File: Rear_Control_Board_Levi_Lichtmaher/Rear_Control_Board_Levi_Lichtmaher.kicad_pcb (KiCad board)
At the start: 2 copper layers, 149.2 x 106.5 mm, 92 parts, among them J1 430450200, J10 Molex Micro-Fit 4 Pin, J11 22035035, J12 22035035, J2 430450200, J3 430450200, J4 430450200, J5 430450200, J6 430450200, J7 430450200, J8 430450200, J9 22035035, Q1 PSMN1R8-40YLC_115, Q2 PSMN1R8-40YLC_115, Q3 PSMN1R8-40YLC_115, Q4 PSMN1R8-40YLC_115, U11 MCP6286T-E/OT, U12 MCP6286T-E/OT, U3 MCP2562-E/P, U4 UA78M05QDCYRG4Q1, U5 ASM330LHHTR, U6 MCP6286T-E/OT

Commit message: implemented feedback
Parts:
- added R22: 2K, Resistor_SMD:R_0805_2012Metric, F.Cu at (187.3, 102.3)
- added R23: 1K, Resistor_SMD:R_0805_2012Metric, F.Cu at (187.3, 98.7)
- TP35: value 2V5 -> 2V2
- moved TP35 76.2 mm to (189.6, 99.7)
- moved C1 10.2 mm to (103.0, 52.0), turned to 90 degrees
- moved C3 8.67 mm to (99.3, 52.7)
- moved TP15 5.20 mm to (200.1, 92.8)
- moved TP18 4.79 mm to (188.0, 108.3)
- moved TP7 4.13 mm to (96.0, 55.0)
- moved U4 2.22 mm to (100.7, 58.1), turned to 180 degrees
- moved J2 0.77 mm to (191.6, 46.9)
- moved C2 0.71 mm to (181.1, 104.8)
- moved R17 0.67 mm to (179.1, 104.9)
- moved U2 0.49 mm to (179.9, 109.8)
- moved R19 0.35 mm to (180.5, 100.5)
- moved R12 0.05 mm to (180.5, 98.5)
- renumbered 3.3V to TP12, 2.4V to TP18, 5V to TP2, 2.4V to TP21, 12V to TP27, 12V to TP36, GND to TP43, ADC to U2
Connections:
- net +2V5 renamed Net-(U2-AIN3)
- U4 pad 1: +5V -> +12V
- U4 pad 3: +12V -> +5V
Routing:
- net Net-(U2-AIN3): track 0.00 -> 15.6 mm
- net /MISO: track 1.90 -> 14.5 mm
- net +5V: track 135.4 -> 142.6 mm
- net /SCK: track 39.4 -> 33.9 mm, vias 2 -> 0
- net Net-(U7-PB14): track 12.3 -> 8.14 mm
- net +3V3: track 283.9 -> 280.1 mm
- net /Pressure: track 25.7 -> 29.0 mm
- net +12V: track 276.1 -> 273.2 mm
- net Net-(J9-Pad3): track 9.61 -> 6.70 mm
- net GND: track 81.4 -> 79.7 mm, vias 37 -> 38
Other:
- board text added: "2.2V"
- board text added: "2.4V"
- board text added: "3.3V"
- board text added: "LDO"
- board text added: "MOSFET"
- board text added: "TP7"
- board text removed: "IDK what to do with this and IDK where to get 2.5V"
- board text removed: "TP12"
- board text removed: "TP18"
- board text removed: "TP2"
- board text removed: "TP21"
- board text removed: "TP27"
- board text removed: "TP36"
- board text removed: "TP43"

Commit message: made board smaller, cleaned up silkscreen
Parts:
- moved REF** 70.8 mm to (78.2, 64.0)
- moved H4 19.4 mm to (207.0, 121.0)
- moved H3 19.0 mm to (74.0, 121.0)
- moved TP37 15.3 mm to (180.8, 52.7)
- moved C19 6.55 mm to (186.3, 84.0)
- moved C22 6.55 mm to (182.3, 86.5)
- moved R9 6.55 mm to (185.8, 87.5)
- moved U6 6.55 mm to (189.3, 86.2)
- moved C7 6.55 mm to (193.3, 84.5)
- moved R15 6.55 mm to (192.3, 90.4)
- moved R16 6.55 mm to (188.3, 90.4)
- moved J9 6.55 mm to (197.8, 85.4)
- moved TP14 6.55 mm to (192.5, 87.5)
- moved TP15 6.55 mm to (193.6, 92.4)
- moved H2 4.11 mm to (207.0, 46.5)
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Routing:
- net +12V: track 273.2 -> 260.4 mm
- net +5V: track 142.6 -> 136.5 mm
- net +3V3: track 280.1 -> 276.9 mm
- net GND: track 79.7 -> 82.8 mm
- net /Pressure: track 29.0 -> 32.1 mm
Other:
- board size 149.2 x 106.5 mm -> 143.7 x 84.4 mm
- board text added: "ADC"
- board text added: "CAN Tranciever"
- board text added: "Rear Control Board 01/03/2025 University of California, Los Angeles By Levi Lichtmaher"
- board text removed: "Rear Control Board 12/27/2025 University of California, Los Angeles By Levi Lichtmaher"
- board text removed: "This feels like empty space can i put cool images here or smth"

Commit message: cleaned some stuff up
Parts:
- moved TP43 0.45 mm to (90.2, 51.2)
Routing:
- net GND: track 82.8 -> 81.4 mm, vias 38 -> 37
- net +12V: track 260.4 -> 261.1 mm
- net +3V3: track 276.9 -> 277.5 mm
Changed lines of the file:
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@@
 	(footprint "TestPoint:TestPoint_Pad_D1.0mm"
 		(layer "F.Cu")
-		(at 90.649999 51.25)
+		(at 90.2 51.25)
 		(descr "SMD pad as test Point, diameter 1.0mm")
 		(tags "test point SMD pad")
@@
 	)
 	(segment
-		(start 87.200001 45.825)
-		(end 88.800001 44.225)
-		(width 1)
-		(layer "F.Cu")
-		(net 1)
-	)
-	(segment
 		(start 87.200001 91.1416)
 		(end 87.200001 100.175)
@@
 	)
 	(segment
-		(start 101.549 53.3735)
-		(end 102.975 54.7995)
-		(width 1)
-		(layer "F.Cu")
-		(net 1)
-	)
-	(segment
 		(start 87.200001 73.175)
 		(end 87.200001 81.6416)
@@
 	)
 	(segment
-		(start 88.800001 44.225)
-		(end 98.276844 44.225)
+		(start 89.600001 43.425)
+		(end 97.476844 43.425)
 		(width 1)
 		(layer "F.Cu")
@@
 	)
 	(segment
+		(start 101.549 47.497156)
+		(end 101.549 53.3735)
+		(width 1)
+		(layer "F.Cu")
+		(net 1)
+	)
+	(segment
 		(start 199.57205 52.14705)
 		(end 203.5 56.075)
@@
 	)
 	(segment
+		(start 87.200001 45.825)
+		(end 89.600001 43.425)
+		(width 1)
+		(layer "F.Cu")
+		(net 1)
+	)
+	(segment
 		(start 203.5 56.075)
 		(end 203.5 94)
@@
 	)
 	(segment
-		(start 101.549 47.497156)
-		(end 101.549 53.3735)
+		(start 203.5 94)
+		(end 201 96.5)
 		(width 1)
 		(layer "F.Cu")
@@
 	)
 	(segment
-		(start 203.5 94)
-		(end 201 96.5)
+		(start 97.476844 43.425)
+		(end 101.549 47.497156)
+		(width 1)
+		(layer "F.Cu")
+		(net 1)
+	)
+	(segment
+		(start 101.549 53.3735)
+		(end 102.975 54.7995)
 		(width 1)
 		(layer "F.Cu")
@@
 	)
 	(segment
-		(start 98.276844 44.225)
-		(end 101.549 47.497156)
-		(width 1)
-		(layer "F.Cu")
-		(net 1)
-	)
-	(segment
 		(start 87.200001 68)
 		(end 87.200001 73.175)
@@
 	)
 	(segment
-		(start 181.480174 94.480174)
-		(end 181.480174 94.966511)
-		(width 0.2)
-		(layer "F.Cu")
-		(net 2)
-	)
-	(segment
 		(start 100.25 52.675)
 		(end 100.25 54.54355)
@@
 	)
 	(segment
-		(start 90.649999 45.825)
-		(end 90.649999 51.25)
+		(start 90.2 45.825)
+		(end 90.2 51.25)
 		(width 0.2)
 		(layer "F.Cu")
@@
 	)
 	(segment
-		(start 180.042924 95.24685)
-		(end 181.462498 95.24685)
-		(width 0.2)
-		(layer "F.Cu")
-		(net 2)
-	)
-	(segment
 		(start 200.712501 115.6)
 		(end 200.7 115.587499)
@@
 	)
 	(segment
-		(start 181 94)
-		(end 181.480174 94.480174)
-		(width 0.2)
-		(layer "F.Cu")
-		(net 2)
-	)
-	(segment
 		(start 181.9803 94.966511)
 		(end 181.480174 94.966511)
@@
 	)
 	(segment
+		(start 181.480174 94.480174)
+		(end 181.480174 94.966511)
+		(width 0.2)
+		(layer "F.Cu")
+		(net 2)
+	)
+	(segment
 		(start 100.25 54.54355)
 		(end 100.6636 54.95715)
@@
 	)
 	(segment
+		(start 181 94)
+		(end 181.480174 94.480174)
+		(width 0.2)
+		(layer "F.Cu")
+		(net 2)
+	)
+	(segment
 		(start 100.025 51.05)
 		(end 100.225 51.25)
@@
 	)
 	(via
-		(at 181.462498 95.24685)
-		(size 0.6)
-		(drill 0.3)
-		(layers "F.Cu" "B.Cu")
-		(net 2)
-	)
-	(via
 		(at 100.85 102.075)
 		(size 0.6)
@@
 	)
 	(segment
-		(start 175.687501 110.275)
-		(end 177 111.587499)
+		(start 182.875 98.148785)
+		(end 182.875 101.9)
 		(width 0.2)
 		(layer "F.Cu")
@@
 	)
 	(segment
-		(start 170.6 103.3579)
-		(end 170.6 109.4)
+		(start 181.9803 96.733111)
+		(end 181.9803 97.254085)
 		(width 0.2)
 		(layer "F.Cu")
@@
 	)
 	(segment
-		(start 181.9803 96.733111)
-		(end 181.9803 97.254085)
+		(start 170.6 103.3579)
+		(end 170.6 109.125)
 		(width 0.2)
 		(layer "F.Cu")
@@
 	)
 	(segment
-		(start 182.232 102.543)
-		(end 171.4149 102.543)
+		(start 175.687501 110.275)
+		(end 177 111.587499)
 		(width 0.2)
 		(layer "F.Cu")
@@
 	)
 	(segment
-		(start 182.875 98.148785)
-		(end 182.875 101.9)
+		(start 178.437499 111.587499)
+		(end 178.924999 112.074999)
 		(width 0.2)
 		(layer "F.Cu")
@@
 	)
 	(segment
-		(start 178.437499 111.587499)
-		(end 178.924999 112.074999)
+		(start 171.4149 102.543)
+		(end 170.6 103.3579)
 		(width 0.2)
 		(layer "F.Cu")
@@
 	)
 	(segment
-		(start 181.9803 97.254085)
-		(end 182.875 98.148785)
+		(start 182.875 101.9)
+		(end 182.232 102.543)
 		(width 0.2)
 		(layer "F.Cu")
@@
 	)
 	(segment
-		(start 182.875 101.9)
-		(end 182.232 102.543)
+		(start 181.9803 97.254085)
+		(end 182.875 98.148785)
 		(width 0.2)
 		(layer "F.Cu")
@@
 	)
 	(segment
-		(start 171.475 110.275)
-		(end 175.687501 110.275)
+		(start 182.232 102.543)
+		(end 171.4149 102.543)
 		(width 0.2)
 		(layer "F.Cu")
@@
 	)
 	(segment
-		(start 171.4149 102.543)
-		(end 170.6 103.3579)
+		(start 170.6 109.125)
+		(end 171.75 110.275)
 		(width 0.2)
 		(layer "F.Cu")
@@
 	)
 	(segment
-		(start 170.6 109.4)
-		(end 171.475 110.275)
+		(start 171.75 110.275)
+		(end 175.687501 110.275)
 		(width 0.2)
 		(layer "F.Cu")
@@
 	)
 	(segment
-		(start 120.8 79.9)
-		(end 141.675 100.775)
-		(width 0.5)
-		(layer "F.Cu")
-		(net 16)
-	)
-	(segment
 		(start 188.575 113.25)
 		(end 188.589208 113.25)
@@
 	)
 	(segment
+		(start 118.225 77.325)
+		(end 141.675 100.775)
+		(width 0.5)
+		(layer "F.Cu")
+		(net 16)
+	)
+	(segment
 		(start 195.967301 117.699999)
 		(end 195.967301 115.662501)
@@
 	)
 	(segment
-		(start 179.3303 95.099622)
-		(end 179.005426 94.774748)
-		(width 0.5)
-		(layer "F.Cu")
-		(net 16)
-	)
-	(segment
 		(start 120.95 121.5)
 		(end 141.675 100.775)
@@
 	)
 	(segment
+		(start 109.86 77.325)
+		(end 118.225 77.325)
+		(width 0.5)
+		(layer "F.Cu")
+		(net 16)
+	)
+	(segment
 		(start 104.449938 92.700062)
 		(end 104.125 93.025)
@@
 	)
 	(segment
-		(start 108.575 78.61)
-		(end 109.865 79.9)
-		(width 0.5)
-		(layer "F.Cu")
-		(net 16)
-	)
-	(segment
 		(start 184.680426 97.675)
 		(end 184.680426 102.948806)
@@
 	)
 	(segment
-		(start 109.865 79.9)
-		(end 120.8 79.9)
-		(width 0.5)
-		(layer "F.Cu")
-		(net 16)
-	)
-	(segment
 		(start 176.525 81.105)
 		(end 177.705 79.925)
@@
 		(width 0.5)
 		(layer "F.Cu")
+		(net 16)
+	)
+	(segment
+		(start 108.575 78.61)
+		(end 109.86 77.325)
+		(width 0.5)
+		(layer "F.Cu")

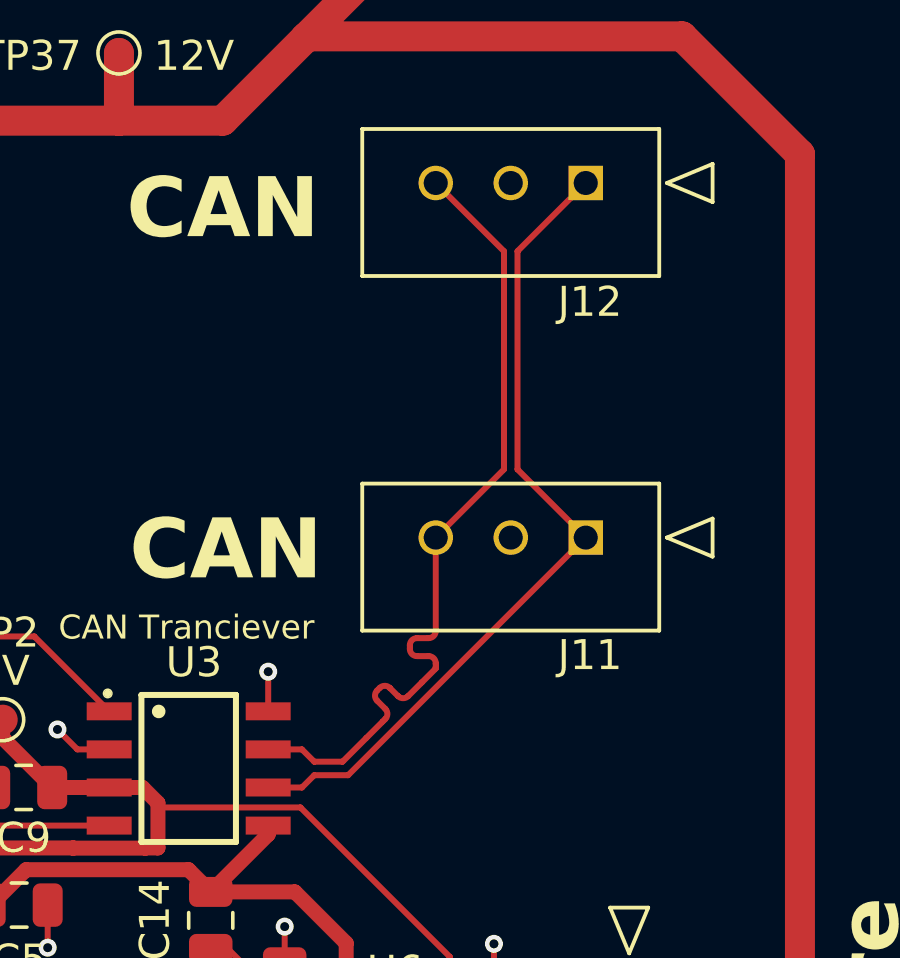
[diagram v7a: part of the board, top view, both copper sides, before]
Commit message: rerouted differential traced for CAN
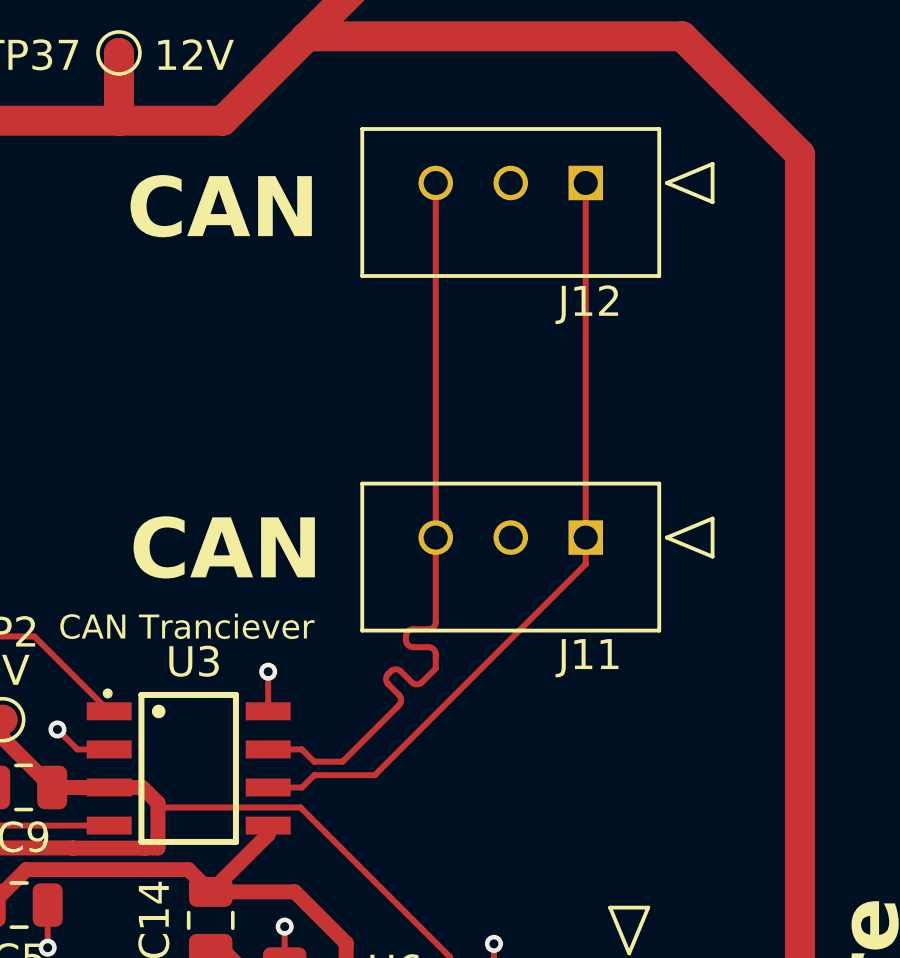
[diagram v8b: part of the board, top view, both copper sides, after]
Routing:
- net /CAN_N: track 27.7 -> 26.4 mm
- net /CAN_P: track 27.7 -> 26.3 mm
